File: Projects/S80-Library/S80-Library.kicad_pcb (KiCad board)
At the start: 2 copper layers, 76.2 x 73.7 mm, 2 parts, among them U1 ATmega328P-PU

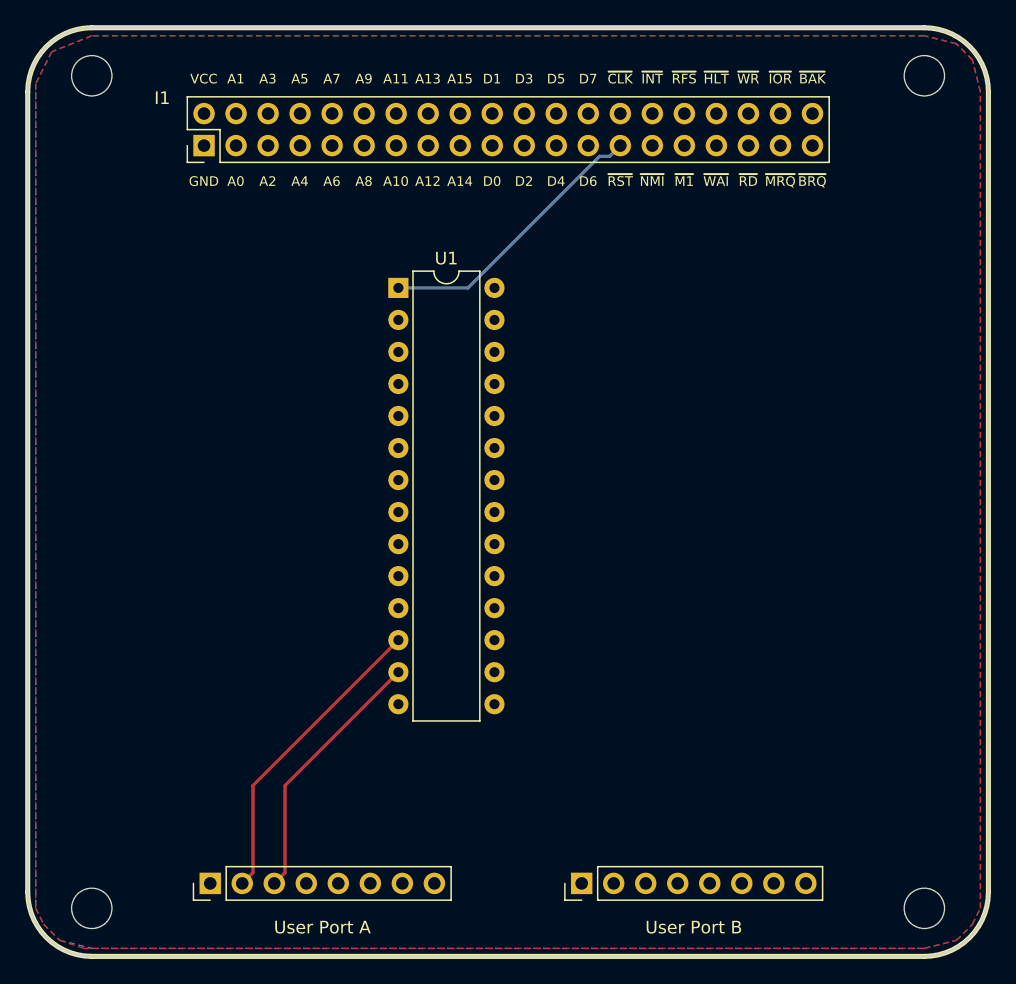
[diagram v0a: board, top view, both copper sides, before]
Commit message: added the template
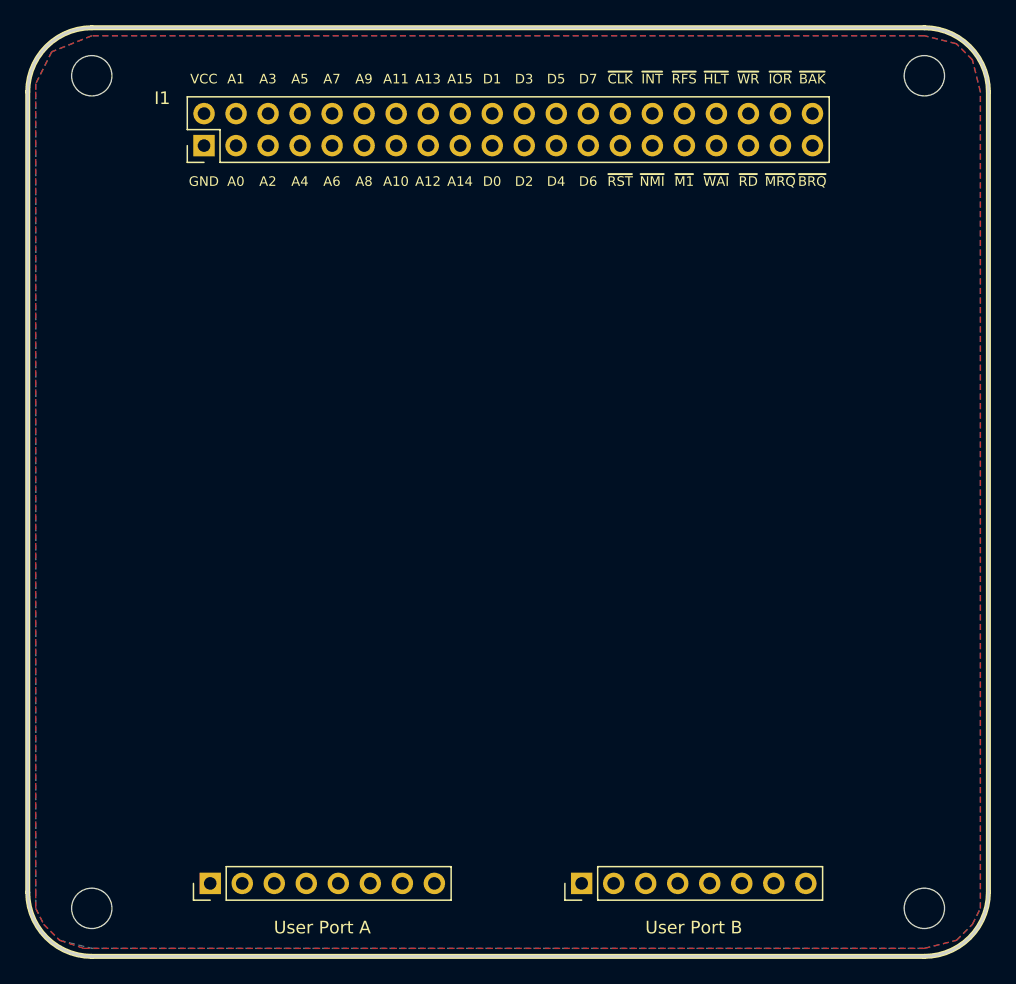
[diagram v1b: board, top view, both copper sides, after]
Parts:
- removed U1: ATmega328P-PU, Housings_DIP:DIP-28_W7.62mm
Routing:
- net Net-(I1-Pad42): track 24.4 -> 0.00 mm
- net Net-(I1-Pad27): track 22.3 -> 0.00 mm
- net Net-(I1-Pad43): track 20.8 -> 0.00 mm
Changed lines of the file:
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@@
     (thickness 1.6)
     (drawings 8)
-    (tracks 12)
+    (tracks 0)
     (zones 0)
-    (modules 2)
-    (nets 79)
+    (modules 1)
+    (nets 57)
   )
   (page A4)
@@
     (solder_mask_min_width 0.25)
     (aux_axis_origin 0 0)
-    (visible_elements FFFFFF7F)
+    (visible_elements 7FFFFFFF)
     (pcbplotparams
       (layerselection 0x010fc_ffffffff)
@@
   (net 55 "Net-(I1-Pad51)")
   (net 56 "Net-(I1-Pad53)")
-  (net 57 "Net-(U1-Pad28)")
-  (net 58 "Net-(U1-Pad14)")
-  (net 59 "Net-(U1-Pad27)")
-  (net 60 "Net-(U1-Pad26)")
-  (net 61 "Net-(U1-Pad25)")
-  (net 62 "Net-(U1-Pad11)")
-  (net 63 "Net-(U1-Pad24)")
-  (net 64 "Net-(U1-Pad10)")
-  (net 65 "Net-(U1-Pad23)")
-  (net 66 "Net-(U1-Pad9)")
-  (net 67 "Net-(U1-Pad21)")
-  (net 68 "Net-(U1-Pad20)")
-  (net 69 "Net-(U1-Pad6)")
-  (net 70 "Net-(U1-Pad19)")
-  (net 71 "Net-(U1-Pad5)")
-  (net 72 "Net-(U1-Pad18)")
-  (net 73 "Net-(U1-Pad4)")
-  (net 74 "Net-(U1-Pad17)")
-  (net 75 "Net-(U1-Pad3)")
-  (net 76 "Net-(U1-Pad16)")
-  (net 77 "Net-(U1-Pad2)")
-  (net 78 "Net-(U1-Pad15)")
   (net_class Default "This is the default net class."
     (clearance 0.2)
@@
     (add_net "Net-(I1-Pad8)")
     (add_net "Net-(I1-Pad9)")
-    (add_net "Net-(U1-Pad10)")
-    (add_net "Net-(U1-Pad11)")
-    (add_net "Net-(U1-Pad14)")
-    (add_net "Net-(U1-Pad15)")
-    (add_net "Net-(U1-Pad16)")
-    (add_net "Net-(U1-Pad17)")
-    (add_net "Net-(U1-Pad18)")
-    (add_net "Net-(U1-Pad19)")
-    (add_net "Net-(U1-Pad2)")
-    (add_net "Net-(U1-Pad20)")
-    (add_net "Net-(U1-Pad21)")
-    (add_net "Net-(U1-Pad23)")
-    (add_net "Net-(U1-Pad24)")
-    (add_net "Net-(U1-Pad25)")
-    (add_net "Net-(U1-Pad26)")
-    (add_net "Net-(U1-Pad27)")
-    (add_net "Net-(U1-Pad28)")
-    (add_net "Net-(U1-Pad3)")
-    (add_net "Net-(U1-Pad4)")
-    (add_net "Net-(U1-Pad5)")
-    (add_net "Net-(U1-Pad6)")
-    (add_net "Net-(U1-Pad9)")
     (add_net VCC)
   )
@@
     (pad "" np_thru_hole circle (at -33.02 33.02) (size 3.2 3.2) (drill 3.2) (layers *.Cu *.Mask))
   )
-  (module Housings_DIP:DIP-28_W7.62mm (layer F.Cu)
-    (at 151.3205 93.0275)
-    (descr "28-lead though-hole mounted DIP package, row spacing 7.62 mm (300 mils)")
-    (tags "THT DIP DIL PDIP 2.54mm 7.62mm 300mil")
-    (fp_text reference U1 (at 3.81 -2.33) (layer F.SilkS)
-      (effects (font (size 1 1) (thickness 0.15)))
-    )
-    (fp_text value ATmega328P-PU (at 3.81 35.35) (layer F.Fab)
-      (effects (font (size 1 1) (thickness 0.15)))
-    )
-    (fp_text user %R (at 3.81 16.51) (layer F.Fab)
-      (effects (font (size 1 1) (thickness 0.15)))
-    )
-    (fp_line (start 8.7 -1.55) (end -1.1 -1.55) (layer F.CrtYd) (width 0.05))
-    (fp_line (start 8.7 34.55) (end 8.7 -1.55) (layer F.CrtYd) (width 0.05))
-    (fp_line (start -1.1 34.55) (end 8.7 34.55) (layer F.CrtYd) (width 0.05))
-    (fp_line (start -1.1 -1.55) (end -1.1 34.55) (layer F.CrtYd) (width 0.05))
-    (fp_line (start 6.46 -1.33) (end 4.81 -1.33) (layer F.SilkS) (width 0.12))
-    (fp_line (start 6.46 34.35) (end 6.46 -1.33) (layer F.SilkS) (width 0.12))
-    (fp_line (start 1.16 34.35) (end 6.46 34.35) (layer F.SilkS) (width 0.12))
-    (fp_line (start 1.16 -1.33) (end 1.16 34.35) (layer F.SilkS) (width 0.12))
-    (fp_line (start 2.81 -1.33) (end 1.16 -1.33) (layer F.SilkS) (width 0.12))
-    (fp_line (start 0.635 -0.27) (end 1.635 -1.27) (layer F.Fab) (width 0.1))
-    (fp_line (start 0.635 34.29) (end 0.635 -0.27) (layer F.Fab) (width 0.1))
-    (fp_line (start 6.985 34.29) (end 0.635 34.29) (layer F.Fab) (width 0.1))
-    (fp_line (start 6.985 -1.27) (end 6.985 34.29) (layer F.Fab) (width 0.1))
-    (fp_line (start 1.635 -1.27) (end 6.985 -1.27) (layer F.Fab) (width 0.1))
-    (fp_arc (start 3.81 -1.33) (end 2.81 -1.33) (angle -180) (layer F.SilkS) (width 0.12))
-    (pad 28 thru_hole oval (at 7.62 0) (size 1.6 1.6) (drill 0.8) (layers *.Cu *.Mask)
-      (net 57 "Net-(U1-Pad28)"))
-    (pad 14 thru_hole oval (at 0 33.02) (size 1.6 1.6) (drill 0.8) (layers *.Cu *.Mask)
-      (net 58 "Net-(U1-Pad14)"))
-    (pad 27 thru_hole oval (at 7.62 2.54) (size 1.6 1.6) (drill 0.8) (layers *.Cu *.Mask)
-      (net 59 "Net-(U1-Pad27)"))
-    (pad 13 thru_hole oval (at 0 30.48) (size 1.6 1.6) (drill 0.8) (layers *.Cu *.Mask)
-      (net 48 "Net-(I1-Pad43)"))
-    (pad 26 thru_hole oval (at 7.62 5.08) (size 1.6 1.6) (drill 0.8) (layers *.Cu *.Mask)
-      (net 60 "Net-(U1-Pad26)"))
-    (pad 12 thru_hole oval (at 0 27.94) (size 1.6 1.6) (drill 0.8) (layers *.Cu *.Mask)
-      (net 46 "Net-(I1-Pad42)"))
-    (pad 25 thru_hole oval (at 7.62 7.62) (size 1.6 1.6) (drill 0.8) (layers *.Cu *.Mask)
-      (net 61 "Net-(U1-Pad25)"))
-    (pad 11 thru_hole oval (at 0 25.4) (size 1.6 1.6) (drill 0.8) (layers *.Cu *.Mask)
-      (net 62 "Net-(U1-Pad11)"))
-    (pad 24 thru_hole oval (at 7.62 10.16) (size 1.6 1.6) (drill 0.8) (layers *.Cu *.Mask)
-      (net 63 "Net-(U1-Pad24)"))
-    (pad 10 thru_hole oval (at 0 22.86) (size 1.6 1.6) (drill 0.8) (layers *.Cu *.Mask)
-      (net 64 "Net-(U1-Pad10)"))
-    (pad 23 thru_hole oval (at 7.62 12.7) (size 1.6 1.6) (drill 0.8) (layers *.Cu *.Mask)
-      (net 65 "Net-(U1-Pad23)"))
-    (pad 9 thru_hole oval (at 0 20.32) (size 1.6 1.6) (drill 0.8) (layers *.Cu *.Mask)
-      (net 66 "Net-(U1-Pad9)"))
-    (pad 22 thru_hole oval (at 7.62 15.24) (size 1.6 1.6) (drill 0.8) (layers *.Cu *.Mask)
-      (net 4 GND))
-    (pad 8 thru_hole oval (at 0 17.78) (size 1.6 1.6) (drill 0.8) (layers *.Cu *.Mask)
-      (net 4 GND))
-    (pad 21 thru_hole oval (at 7.62 17.78) (size 1.6 1.6) (drill 0.8) (layers *.Cu *.Mask)
-      (net 67 "Net-(U1-Pad21)"))
-    (pad 7 thru_hole oval (at 0 15.24) (size 1.6 1.6) (drill 0.8) (layers *.Cu *.Mask)
-      (net 10 VCC))
-    (pad 20 thru_hole oval (at 7.62 20.32) (size 1.6 1.6) (drill 0.8) (layers *.Cu *.Mask)
-      (net 68 "Net-(U1-Pad20)"))
-    (pad 6 thru_hole oval (at 0 12.7) (size 1.6 1.6) (drill 0.8) (layers *.Cu *.Mask)
-      (net 69 "Net-(U1-Pad6)"))
-    (pad 19 thru_hole oval (at 7.62 22.86) (size 1.6 1.6) (drill 0.8) (layers *.Cu *.Mask)
-      (net 70 "Net-(U1-Pad19)"))
-    (pad 5 thru_hole oval (at 0 10.16) (size 1.6 1.6) (drill 0.8) (layers *.Cu *.Mask)
-      (net 71 "Net-(U1-Pad5)"))
-    (pad 18 thru_hole oval (at 7.62 25.4) (size 1.6 1.6) (drill 0.8) (layers *.Cu *.Mask)
-      (net 72 "Net-(U1-Pad18)"))
-    (pad 4 thru_hole oval (at 0 7.62) (size 1.6 1.6) (drill 0.8) (layers *.Cu *.Mask)
-      (net 73 "Net-(U1-Pad4)"))
-    (pad 17 thru_hole oval (at 7.62 27.94) (size 1.6 1.6) (drill 0.8) (layers *.Cu *.Mask)
-      (net 74 "Net-(U1-Pad17)"))
-    (pad 3 thru_hole oval (at 0 5.08) (size 1.6 1.6) (drill 0.8) (layers *.Cu *.Mask)
-      (net 75 "Net-(U1-Pad3)"))
-    (pad 16 thru_hole oval (at 7.62 30.48) (size 1.6 1.6) (drill 0.8) (layers *.Cu *.Mask)
-      (net 76 "Net-(U1-Pad16)"))
-    (pad 2 thru_hole oval (at 0 2.54) (size 1.6 1.6) (drill 0.8) (layers *.Cu *.Mask)
-      (net 77 "Net-(U1-Pad2)"))
-    (pad 15 thru_hole oval (at 7.62 33.02) (size 1.6 1.6) (drill 0.8) (layers *.Cu *.Mask)
-      (net 78 "Net-(U1-Pad15)"))
-    (pad 1 thru_hole rect (at 0 0) (size 1.6 1.6) (drill 0.8) (layers *.Cu *.Mask)
-      (net 26 "Net-(I1-Pad27)"))
-    (model ${KISYS3DMOD}/Housings_DIP.3dshapes/DIP-28_W7.62mm.wrl
-      (at (xyz 0 0 0))
-      (scale (xyz 1 1 1))
-      (rotate (xyz 0 0 0))
-    )
-  )
   (gr_arc (start 127 77.47) (end 127 72.39) (angle -90) (layer Edge.Cuts) (width 0.2))
   (gr_arc (start 127 140.97) (end 121.92 140.97) (angle -90) (layer Edge.Cuts) (width 0.2))
@@
   (gr_line (start 121.92 77.47) (end 121.92 140.97) (layer Edge.Cuts) (width 0.2))
   (gr_line (start 193.04 72.39) (end 127 72.39) (layer Edge.Cuts) (width 0.2))
-  (segment (start 168.075634 82.589999) (end 168.925633 81.74) (width 0.25) (layer B.Cu) (net 26))
-  (segment (start 167.274636 82.589999) (end 168.075634 82.589999) (width 0.25) (layer B.Cu) (net 26))
-  (segment (start 156.837135 93.0275) (end 167.274636 82.589999) (width 0.25) (layer B.Cu) (net 26))
-  (segment (start 151.3205 93.0275) (end 156.837135 93.0275) (width 0.25) (layer B.Cu) (net 26))
-  (segment (start 150.520501 121.767499) (end 151.3205 120.9675) (width 0.25) (layer F.Cu) (net 46))
-  (segment (start 139.784599 132.503401) (end 150.520501 121.767499) (width 0.25) (layer F.Cu) (net 46))
-  (segment (start 139.784599 139.412001) (end 139.784599 132.503401) (width 0.25) (layer F.Cu) (net 46))
-  (segment (start 138.9346 140.262) (end 139.784599 139.412001) (width 0.25) (layer F.Cu) (net 46))
-  (segment (start 150.520501 124.307499) (end 151.3205 123.5075) (width 0.25) (layer F.Cu) (net 48))
-  (segment (start 142.324599 132.503401) (end 150.520501 124.307499) (width 0.25) (layer F.Cu) (net 48))
-  (segment (start 142.324599 139.412001) (end 142.324599 132.503401) (width 0.25) (layer F.Cu) (net 48))
-  (segment (start 141.4746 140.262) (end 142.324599 139.412001) (width 0.25) (layer F.Cu) (net 48))
   (zone (net 10) (net_name VCC) (layer F.Cu) (hatch edge 0.508)
     (connect_pads (clearance 0.508))
